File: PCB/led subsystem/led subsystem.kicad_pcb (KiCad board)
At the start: 2 copper layers, 100 x 100 mm, 30 parts, among them U1 MCU_Seeed_XIAO_ESP32-C3

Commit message: update motor PCB for hall effect sensor and other stuff
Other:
- board text added: "LED PCB V.1"
- board text removed: "CORE PCB V.1"

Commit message: start led subsystem firmware!
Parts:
- added REF**: TestPoint_THTPad_D2.0mm_Drill1.0mm, TestPoint:TestPoint_THTPad_D2.0mm_Drill1.0mm, F.Cu at (182.5, 95.0)
- added REF**: TestPoint_THTPad_D2.0mm_Drill1.0mm, TestPoint:TestPoint_THTPad_D2.0mm_Drill1.0mm, F.Cu at (183.0, 85.0)
- moved D1 2.57 mm to (189.5, 80.8)
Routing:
- net A3144E GND: track 26.8 -> 82.9 mm
- net unconnected-(U1-PA7_A8_D8_SCK-Pad9): track 0.00 -> 5.30 mm

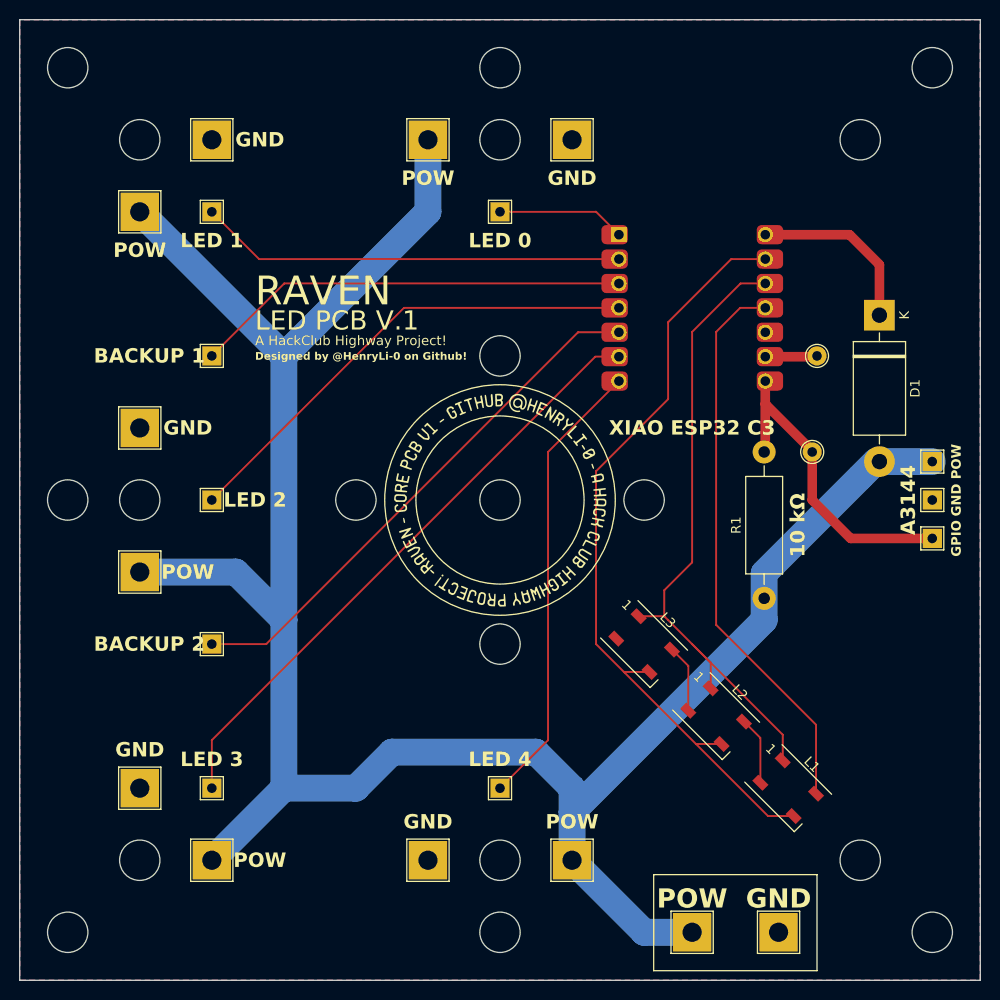
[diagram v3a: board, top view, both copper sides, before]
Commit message: cad, screws, and mounting holes!
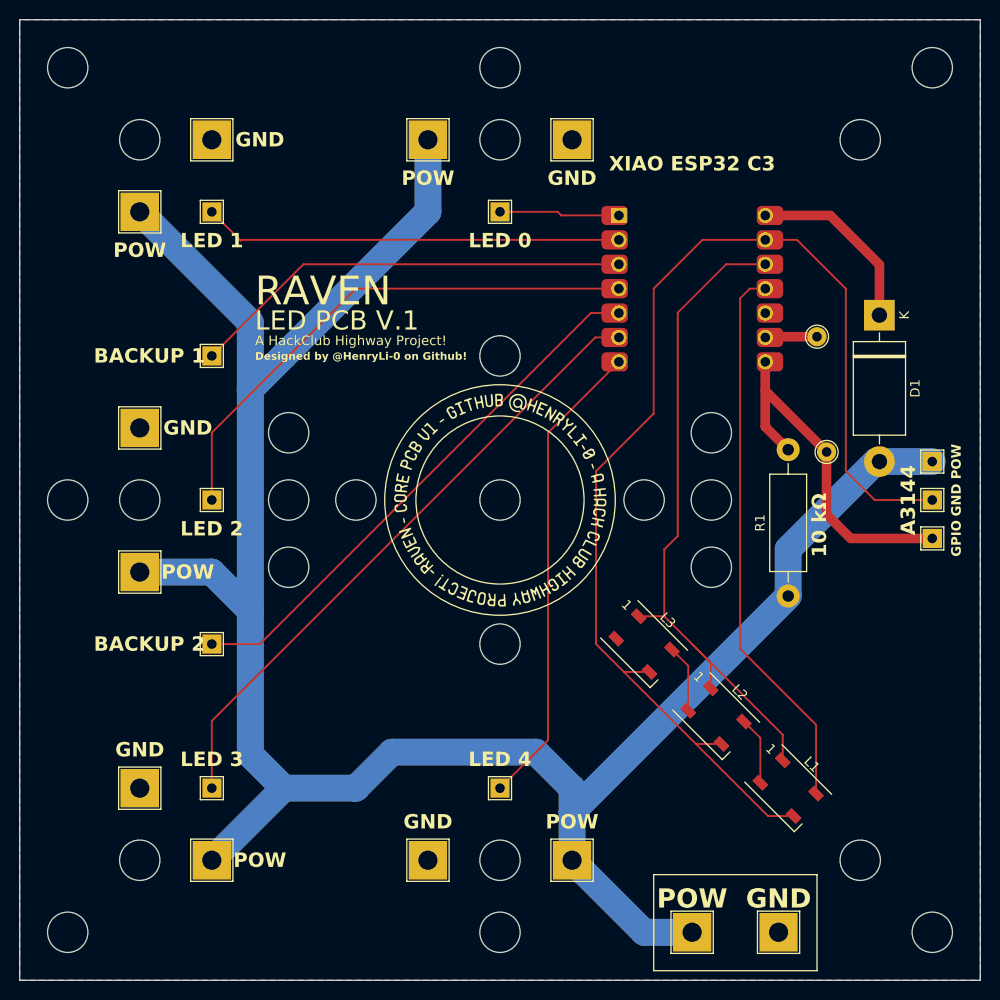
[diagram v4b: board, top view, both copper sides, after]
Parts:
- moved R1 2.51 mm to (180.0, 110.0)
- moved REF** 2.00 mm to (183.0, 83.0)
- moved U1 2.00 mm to (170.0, 78.0)
- moved REF** 1.50 mm to (184.0, 95.0)
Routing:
- net A3144E GND: track 82.9 -> 126.4 mm
- net LED_2: track 50.2 -> 55.6 mm
- net A3144E GPIO: track 33.6 -> 37.7 mm
- net +3V3: track 68.7 -> 71.6 mm
- net LED_4: track 47.5 -> 49.5 mm
- net LED_3: track 63.9 -> 65.9 mm
- net LED_BACKUP_1: track 45.1 -> 46.3 mm
- net A3114E POW: track 234.3 -> 235.3 mm
- net LED_0: track 13.4 -> 12.5 mm
- net Net-(D1-K): track 18.0 -> 18.8 mm
- net LED_BACKUP_2: track 55.8 -> 56.7 mm
- net LED_1: track 44.4 -> 43.7 mm
- net SELF LED: track 58.5 -> 57.9 mm
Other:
- outline, holes or cut-outs redrawn

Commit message: 07172025 - wrapping up CAD!
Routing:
- net A3114E POW: track 235.3 -> 243.7 mm
- net SELF LED: track 57.9 -> 62.0 mm
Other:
- outline, holes or cut-outs redrawn

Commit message: 07182025 - almost done with CAD, lots of writing!
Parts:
- removed the G*** at (150.0, 100.0) (x2)
- added G***: LOGO, LOGO, F.Cu at (150.0, 100.0)
- added G***: LOGO, LOGO, B.Cu at (150.0, 100.0)
- added REF**: TestPoint_THTPad_D2.0mm_Drill1.0mm, TestPoint:TestPoint_THTPad_D2.0mm_Drill1.0mm, F.Cu at (182.5, 79.0)
- moved REF** 17.5 mm to (195.0, 78.5)
- moved REF** 17.5 mm to (195.0, 86.5)
- moved REF** 17.5 mm to (195.0, 82.5)
- moved REF** 9.86 mm to (192.5, 90.0)
- moved D1 6.21 mm to (187.5, 74.9)
- moved R1 4.88 mm to (180.0, 105.1)
- moved REF** 0.50 mm to (182.5, 83.0)
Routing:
- net A3144E GND: track 126.4 -> 108.0 mm
- net A3114E POW: track 243.7 -> 259.8 mm
- net A3144E GPIO: track 37.7 -> 26.2 mm
- net Net-(D1-K): track 18.8 -> 12.7 mm
- net unconnected-(U1-PA5_A9_D9_MISO-Pad10): track 0.00 -> 5.04 mm
- net unconnected-(U1-PA7_A8_D8_SCK-Pad9): track 5.53 -> 4.91 mm
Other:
- outline, holes or cut-outs redrawn

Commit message: 07232025 - mosfet added and writing BOM!
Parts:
- moved R1 2.12 mm to (180.0, 107.2)
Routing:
- net A3144E GPIO: track 26.2 -> 30.0 mm
- net A3114E POW: track 259.8 -> 259.3 mm
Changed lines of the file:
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@@
 	(footprint "Resistor_THT:R_Axial_DIN0411_L9.9mm_D3.6mm_P15.24mm_Horizontal"
 		(layer "F.Cu")
-		(at 180 105.12 90)
+		(at 180 107.24 90)
 		(descr "Resistor, Axial_DIN0411 series, Axial, Horizontal, pin pitch=15.24mm, 1W, length*diameter=9.9*3.6mm^2")
 		(tags "Resistor Axial_DIN0411 series Axial Horizontal pin pitch 15.24mm 1W length 9.9mm diameter 3.6mm")
@@
 		(tags "Diode DO-201AD series Axial Horizontal pin pitch 15.24mm  length 9.5mm diameter 5.2mm")
 		(property "Reference" "D1"
-			(at 7.62 -3.72 90)
+			(at 7.62 -3.5 90)
 			(layer "F.SilkS")
 			(effects
@@
 	)
 	(gr_text "10 kΩ"
-		(at 183 91.88 90)
+		(at 183 95 90)
 		(layer "B.SilkS")
 		(effects
@@
 	)
 	(gr_text "10 kΩ"
-		(at 183 92 90)
+		(at 183 95.12 90)
 		(layer "F.SilkS")
 		(effects
@@
 	)
 	(segment
-		(start 131 89)
-		(end 131 88.5)
-		(width 2.8)
-		(layer "B.Cu")
-		(net 2)
-	)
-	(segment
 		(start 157.5 130)
 		(end 157.5 137.5)
@@
 	)
 	(segment
-		(start 187.5 86.5)
-		(end 195 86.5)
-		(width 1)
-		(layer "F.Cu")
-		(net 8)
-	)
-	(segment
 		(start 192.5 90)
 		(end 189 86.5)
@@
 	)
 	(segment
-		(start 181.5 86.5)
-		(end 180 88)
+		(start 185.5 86.5)
+		(end 180 92)
 		(width 1)
 		(layer "F.Cu")
@@
 	(segment
 		(start 178.1 85.62)
-		(end 180.62 85.62)
-		(width 1)
-		(layer "F.Cu")
-		(net 8)
-	)
-	(segment
-		(start 180.62 85.62)
-		(end 181.5 86.5)
+		(end 184.62 85.62)
 		(width 1)
 		(layer "F.Cu")
@@
 	)
 	(segment
-		(start 180 88)
-		(end 180 89.88)
+		(start 184.62 85.62)
+		(end 185.5 86.5)
 		(width 1)
 		(layer "F.Cu")
@@
 	)
 	(segment
-		(start 181.5 86.5)
-		(end 187.5 86.5)
+		(start 185.5 86.5)
+		(end 195 86.5)
 		(width 1)
 		(layer "F.Cu")

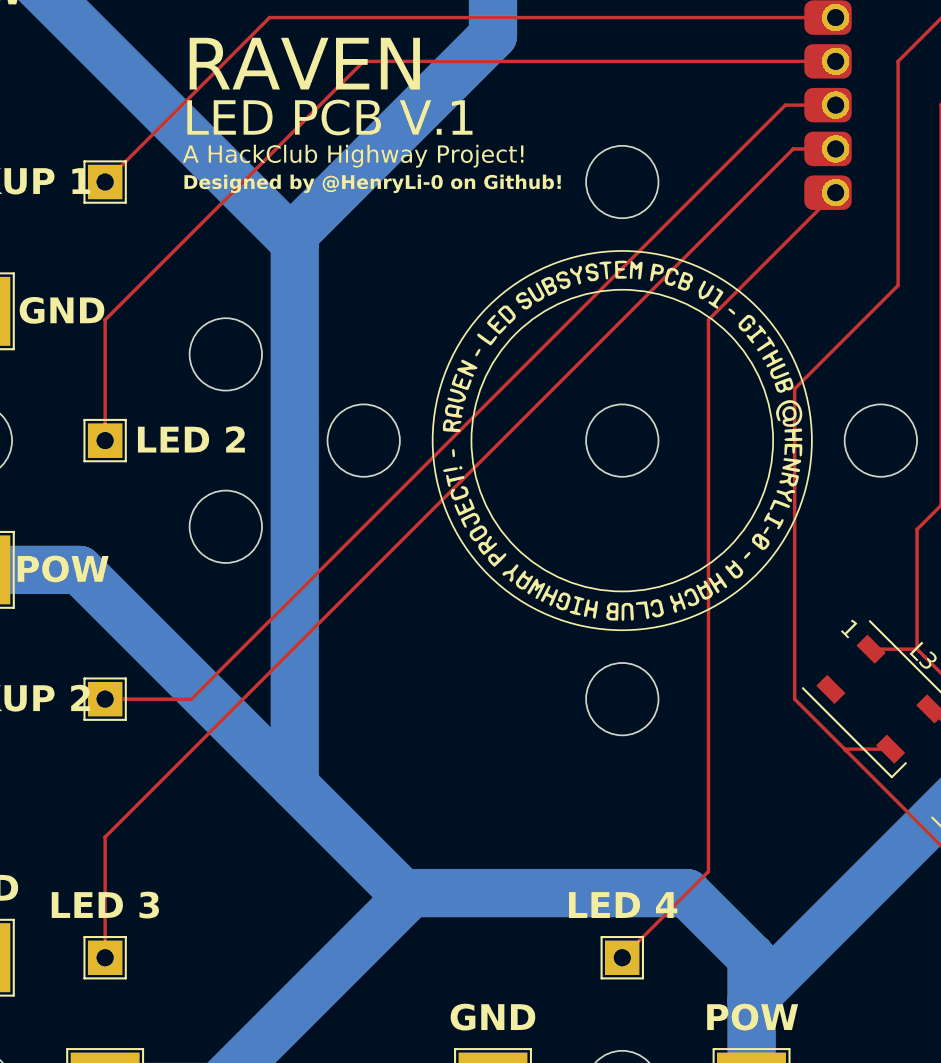
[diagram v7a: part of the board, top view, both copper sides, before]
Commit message: 07242025 - parts and almost finishing BOM!
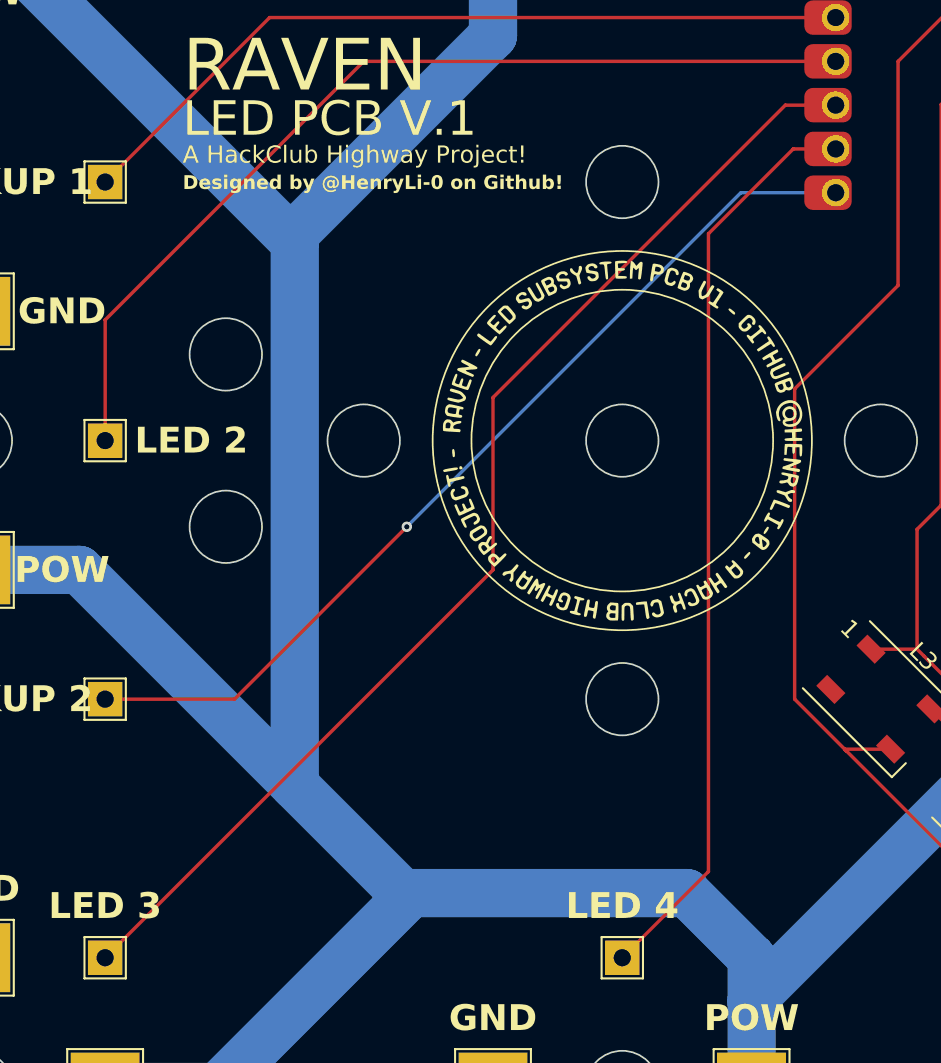
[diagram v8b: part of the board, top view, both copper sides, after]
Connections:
- U1 pad 5: LED_BACKUP_2 -> LED_3
- U1 pad 6: LED_3 -> LED_4
- U1 pad 7: LED_4 -> LED_BACKUP_2
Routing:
- net LED_4: track 49.5 -> 53.0 mm
- net LED_3: track 65.9 -> 68.7 mm
- net LED_BACKUP_2: track 56.7 -> 54.5 mm, vias 0 -> 1
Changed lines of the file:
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@@
 			(layers "F.Cu" "F.Paste" "F.Mask")
 			(roundrect_rratio 0.25)
-			(net 14 "LED_BACKUP_2")
+			(net 10 "LED_3")
 			(pinfunction "PA8_A4_D4_SDA")
 			(pintype "passive")
@@
 			(layers "*.Cu" "*.Mask")
 			(remove_unused_layers no)
-			(net 14 "LED_BACKUP_2")
+			(net 10 "LED_3")
 			(pinfunction "PA8_A4_D4_SDA")
 			(pintype "passive")
@@
 			(layers "F.Cu" "F.Paste" "F.Mask")
 			(roundrect_rratio 0.25)
-			(net 10 "LED_3")
+			(net 9 "LED_4")
 			(pinfunction "PA9_A5_D5_SCL")
 			(pintype "passive")
@@
 			(layers "*.Cu" "*.Mask")
 			(remove_unused_layers no)
-			(net 10 "LED_3")
+			(net 9 "LED_4")
 			(pinfunction "PA9_A5_D5_SCL")
 			(pintype "passive")
@@
 			(layers "F.Cu" "F.Paste" "F.Mask")
 			(roundrect_rratio 0.25)
-			(net 9 "LED_4")
+			(net 14 "LED_BACKUP_2")
 			(pinfunction "PB08_A6_D6_TX")
 			(pintype "passive")
@@
 			(layers "*.Cu" "*.Mask")
 			(remove_unused_layers no)
-			(net 9 "LED_4")
+			(net 14 "LED_BACKUP_2")
 			(pinfunction "PB08_A6_D6_TX")
 			(pintype "passive")
@@
 	(segment
 		(start 155 125)
-		(end 150 130)
+		(end 155 88)
 		(width 0.2)
 		(layer "F.Cu")
@@
 	)
 	(segment
-		(start 155 93)
+		(start 150 130)
 		(end 155 125)
 		(width 0.2)
@@
 	)
 	(segment
-		(start 162.38 85.62)
-		(end 155 93)
+		(start 155 88)
+		(end 159.92 83.08)
 		(width 0.2)
 		(layer "F.Cu")
@@
 	(segment
 		(start 159.92 83.08)
-		(end 120 123)
+		(end 161.935 83.08)
 		(width 0.2)
 		(layer "F.Cu")
-		(net 10)
+		(net 9)
 	)
 	(segment
-		(start 120 123)
+		(start 142.5 107.5)
 		(end 120 130)
 		(width 0.2)
@@
 	)
 	(segment
-		(start 162.38 83.08)
-		(end 159.92 83.08)
+		(start 162.38 80.54)
+		(end 159.46 80.54)
+		(width 0.2)
+		(layer "F.Cu")
+		(net 10)
+	)
+	(segment
+		(start 159.46 80.54)
+		(end 142.5 97.5)
+		(width 0.2)
+		(layer "F.Cu")
+		(net 10)
+	)
+	(segment
+		(start 142.5 97.5)
+		(end 142.5 107.5)
 		(width 0.2)
 		(layer "F.Cu")
@@
 	)
 	(segment
-		(start 159.46 80.54)
-		(end 125 115)
+		(start 120 115)
+		(end 127.5 115)
 		(width 0.2)
 		(layer "F.Cu")
@@
 	)
 	(segment
-		(start 162.38 80.54)
-		(end 159.46 80.54)
+		(start 127.5 115)
+		(end 137.5 105)
 		(width 0.2)
 		(layer "F.Cu")
 		(net 14)
 	)
+	(via
+		(at 137.5 105)
+		(size 0.6)
+		(drill 0.3)
+		(layers "F.Cu" "B.Cu")
+		(net 14)
+	)
 	(segment
-		(start 125 115)
-		(end 120 115)
+		(start 156.88 85.62)
+		(end 162.38 85.62)
 		(width 0.2)
-		(layer "F.Cu")
+		(layer "B.Cu")
+		(net 14)
+	)
+	(segment
+		(start 137.5 105)
+		(end 156.88 85.62)
+		(width 0.2)
+		(layer "B.Cu")
 		(net 14)
 	)
